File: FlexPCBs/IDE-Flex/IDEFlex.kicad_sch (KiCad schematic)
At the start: 18 parts, among them J1 Conn_01x04_Pin, J2 Conn_01x04_Pin, J3 Conn_01x04_Pin, J4 Conn_01x04_Pin, J5 Conn_01x04_Pin, J6 Conn_01x04_Pin, J7 Conn_01x04_Pin, U1 IDE25

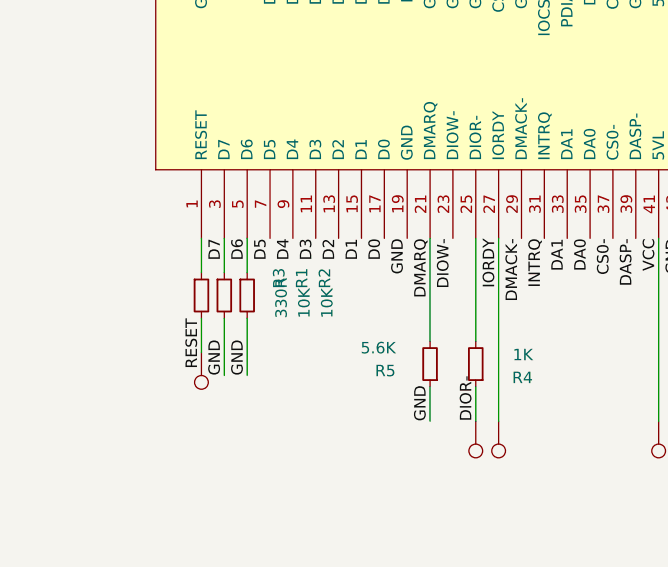
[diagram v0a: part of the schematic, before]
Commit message: Delete HDMI Flipper Design Add HDMI Flex Add USB C/Power and volume button PCB Add Housing CAD Update IDE Flex Update S Controller PCBs Update LPC Flex Update USB Flex
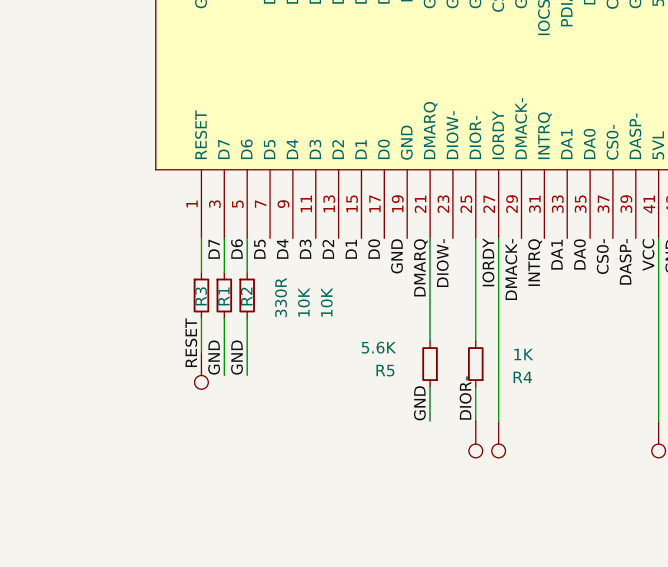
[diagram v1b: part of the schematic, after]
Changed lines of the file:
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@@
 (kicad_sch
-	(version 20240417)
+	(version 20250114)
 	(generator "eeschema")
-	(generator_version "8.99")
+	(generator_version "9.0")
 	(paper "A4")
 	(wire
@@
 	(label "INTRQ"
 		(at 125.73 78.74 270)
-		(fields_autoplaced yes)
 		(effects
 			(font
@@
 	(label "D7"
 		(at 90.17 78.74 270)
-		(fields_autoplaced yes)
 		(effects
 			(font
@@
 	(label "GND"
 		(at 135.89 29.21 270)
-		(fields_autoplaced yes)
 		(effects
 			(font
@@
 	(label "DA2"
 		(at 133.35 123.19 90)
-		(fields_autoplaced yes)
 		(effects
 			(font
@@
 	(label "IORDY"
 		(at 120.65 78.74 270)
-		(fields_autoplaced yes)
 		(effects
 			(font
@@
 	(label "D13"
 		(at 86.36 121.92 90)
-		(fields_autoplaced yes)
 		(effects
 			(font
@@
 	(label "D6"
 		(at 92.71 78.74 270)
-		(fields_autoplaced yes)
 		(effects
 			(font
@@
 	(label "D7"
 		(at 80.01 121.92 90)
-		(fields_autoplaced yes)
 		(effects
 			(font
@@
 	(label "D11"
 		(at 83.82 121.92 90)
-		(fields_autoplaced yes)
 		(effects
 			(font
@@
 	(label "DA0"
 		(at 130.81 78.74 270)
-		(fields_autoplaced yes)
 		(effects
 			(font
@@
 	(label "IOCS16-"
 		(at 125.73 29.21 270)
-		(fields_autoplaced yes)
 		(effects
 			(font
@@
 	(label "D5"
 		(at 95.25 78.74 270)
-		(fields_autoplaced yes)
 		(effects
 			(font
@@
 	(label "D15"
 		(at 95.25 121.92 90)
-		(fields_autoplaced yes)
 		(effects
 			(font
@@
 	(label "D15"
 		(at 107.95 29.21 270)
-		(fields_autoplaced yes)
 		(effects
 			(font
@@
 	(label "D10"
 		(at 95.25 29.21 270)
-		(fields_autoplaced yes)
 		(effects
 			(font
@@
 	(label "D14"
 		(at 105.41 29.21 270)
-		(fields_autoplaced yes)
 		(effects
 			(font
@@
 	(label "D5"
 		(at 162.56 123.19 90)
-		(fields_autoplaced yes)
 		(effects
 			(font
@@
 	(label "INTRQ"
 		(at 139.7 123.19 90)
-		(fields_autoplaced yes)
 		(effects
 			(font
@@
 	(label "D11"
 		(at 97.79 29.21 270)
-		(fields_autoplaced yes)
 		(effects
 			(font
@@
 	(label "D3"
 		(at 88.9 121.92 90)
-		(fields_autoplaced yes)
 		(effects
 			(font
@@
 	(label "GND"
 		(at 113.03 29.21 270)
-		(fields_autoplaced yes)
 		(effects
 			(font
@@
 	(label "D1"
 		(at 151.13 123.19 90)
-		(fields_autoplaced yes)
 		(effects
 			(font
@@
 	(label "DIOW-"
 		(at 148.59 123.19 90)
-		(fields_autoplaced yes)
 		(effects
 			(font
@@
 	(label "DA0"
 		(at 130.81 123.19 90)
-		(fields_autoplaced yes)
 		(effects
 			(font
@@
 	(label "DA1"
 		(at 137.16 123.19 90)
-		(fields_autoplaced yes)
 		(effects
 			(font
@@
 	(label "GND"
 		(at 92.71 93.98 90)
-		(fields_autoplaced yes)
 		(effects
 			(font
@@
 	(label "D14"
 		(at 153.67 123.19 90)
-		(fields_autoplaced yes)
 		(effects
 			(font
@@
 	(label "GND"
 		(at 120.65 29.21 270)
-		(fields_autoplaced yes)
 		(effects
 			(font
@@
 	(label "CS1-"
 		(at 133.35 29.21 270)
-		(fields_autoplaced yes)
 		(effects
 			(font
@@
 	(label "D4"
 		(at 97.79 78.74 270)
-		(fields_autoplaced yes)
 		(effects
 			(font
@@
 	(label "D3"
 		(at 100.33 78.74 270)
-		(fields_autoplaced yes)
 		(effects
 			(font
@@
 	(label "DA1"
 		(at 128.27 78.74 270)
-		(fields_autoplaced yes)
 		(effects
 			(font
@@
 	(label "RESET"
 		(at 87.63 87.63 270)
-		(fields_autoplaced yes)
 		(effects
 			(font
@@
 	(label "GND"
 		(at 123.19 29.21 270)
-		(fields_autoplaced yes)
 		(effects
 			(font
@@
 	(label "D12"
 		(at 100.33 29.21 270)
-		(fields_autoplaced yes)
 		(effects
 			(font
@@
 	(label "CS0-"
 		(at 133.35 78.74 270)
-		(fields_autoplaced yes)
 		(effects
 			(font
@@
 	(label "GND"
 		(at 140.97 78.74 270)
-		(fields_autoplaced yes)
 		(effects
 			(font
@@
 	(label "GND"
 		(at 87.63 29.21 270)
-		(fields_autoplaced yes)
 		(effects
 			(font
@@
 	(label "DMARQ"
 		(at 100.33 121.92 90)
-		(fields_autoplaced yes)
 		(effects
 			(font
@@
 	(label "CS1-"
 		(at 128.27 123.19 90)
-		(fields_autoplaced yes)
 		(effects
 			(font
@@
 	(label "GND"
 		(at 115.57 29.21 270)
-		(fields_autoplaced yes)
 		(effects
 			(font
@@
 	(label "GND"
 		(at 90.17 93.98 90)
-		(fields_autoplaced yes)
 		(effects
 			(font
@@
 	(label "DMARQ"
 		(at 113.03 78.74 270)
-		(fields_autoplaced yes)
 		(effects
 			(font
@@
 	(label "D1"
 		(at 105.41 78.74 270)
-		(fields_autoplaced yes)
 		(effects
 			(font
@@
 	(label "D10"
 		(at 165.1 123.19 90)
-		(fields_autoplaced yes)
 		(effects
 			(font
@@
 	(label "D8"
 		(at 74.93 121.92 90)
-		(fields_autoplaced yes)
 		(effects
 			(font
@@
 	(label "D9"
 		(at 92.71 29.21 270)
-		(fields_autoplaced yes)
 		(effects
 			(font
@@
 	(label "D0"
 		(at 107.95 78.74 270)
-		(fields_autoplaced yes)
 		(effects
 			(font
@@
 	(label "D13"
 		(at 102.87 29.21 270)
-		(fields_autoplaced yes)
 		(effects
 			(font
@@
 	(label "VCC"
 		(at 138.43 78.74 270)
-		(fields_autoplaced yes)
 		(effects
 			(font
@@
 	(label "DIOW-"
 		(at 115.57 78.74 270)
-		(fields_autoplaced yes)
 		(effects
 			(font
@@
 	(label "GND"
 		(at 113.03 99.06 90)
-		(fields_autoplaced yes)
 		(effects
 			(font
@@
 	(label "D4"
 		(at 160.02 123.19 90)
-		(fields_autoplaced yes)
 		(effects
 			(font
@@
 	(label "D0"
 		(at 97.79 121.92 90)
-		(fields_autoplaced yes)
 		(effects
 			(font
@@
 	(label "D9"
 		(at 167.64 123.19 90)
-		(fields_autoplaced yes)
 		(effects
 			(font
@@
 	(label "DIOR-"
 		(at 118.11 99.06 90)
-		(fields_autoplaced yes)
 		(effects
 			(font
@@
 	(label "CS0-"
 		(at 125.73 123.19 90)
-		(fields_autoplaced yes)
 		(effects
 			(font
@@
 	(label "DA2"
 		(at 130.81 29.21 270)
-		(fields_autoplaced yes)
 		(effects
 			(font
@@
 	(label "PDIAG-"
 		(at 128.27 29.21 270)
-		(fields_autoplaced yes)
 		(effects
 			(font
@@
 	(label "D6"
 		(at 77.47 121.92 90)
-		(fields_autoplaced yes)
 		(effects
 			(font
@@
 	(label "GND"
 		(at 110.49 78.74 270)
-		(fields_autoplaced yes)
 		(effects
 			(font
@@
 	(label "GND"
 		(at 118.11 29.21 270)
-		(fields_autoplaced yes)
 		(effects
 			(font
@@
 	(label "D8"
 		(at 90.17 29.21 270)
-		(fields_autoplaced yes)
 		(effects
 			(font
@@
 	(label "DMACK-"
 		(at 123.19 78.74 270)
-		(fields_autoplaced yes)
 		(effects
 			(font
@@
 	(label "D2"
 		(at 102.87 78.74 270)
-		(fields_autoplaced yes)
 		(effects
 			(font
@@
 	(label "D2"
 		(at 156.21 123.19 90)
-		(fields_autoplaced yes)
 		(effects
 			(font
@@
 	(label "DASP-"
 		(at 135.89 78.74 270)
-		(fields_autoplaced yes)
 		(effects
 			(font
@@
 	(label "D12"
 		(at 91.44 121.92 90)
-		(fields_autoplaced yes)
 		(effects
 			(font
@@
 	(label "DMACK-"
 		(at 142.24 123.19 90)
-		(fields_autoplaced yes)
 		(effects
 			(font
@@
 		(dnp no)
 		(property "Reference" "R3"
-			(at 96.266 84.328 90)
+			(at 87.63 86.36 90)
 			(effects
 				(font
@@
 		(dnp no)
 		(property "Reference" "R2"
-			(at 101.346 84.328 90)
+			(at 92.71 86.36 90)
 			(effects
 				(font
@@
 		(dnp no)
 		(property "Reference" "R1"
-			(at 98.806 84.328 90)
+			(at 90.17 86.36 90)
 			(effects
 				(font
@@
 		)
 	)
+	(embedded_fonts no)
 )
